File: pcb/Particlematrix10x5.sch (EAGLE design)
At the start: 67 parts, among them IC1 4017D

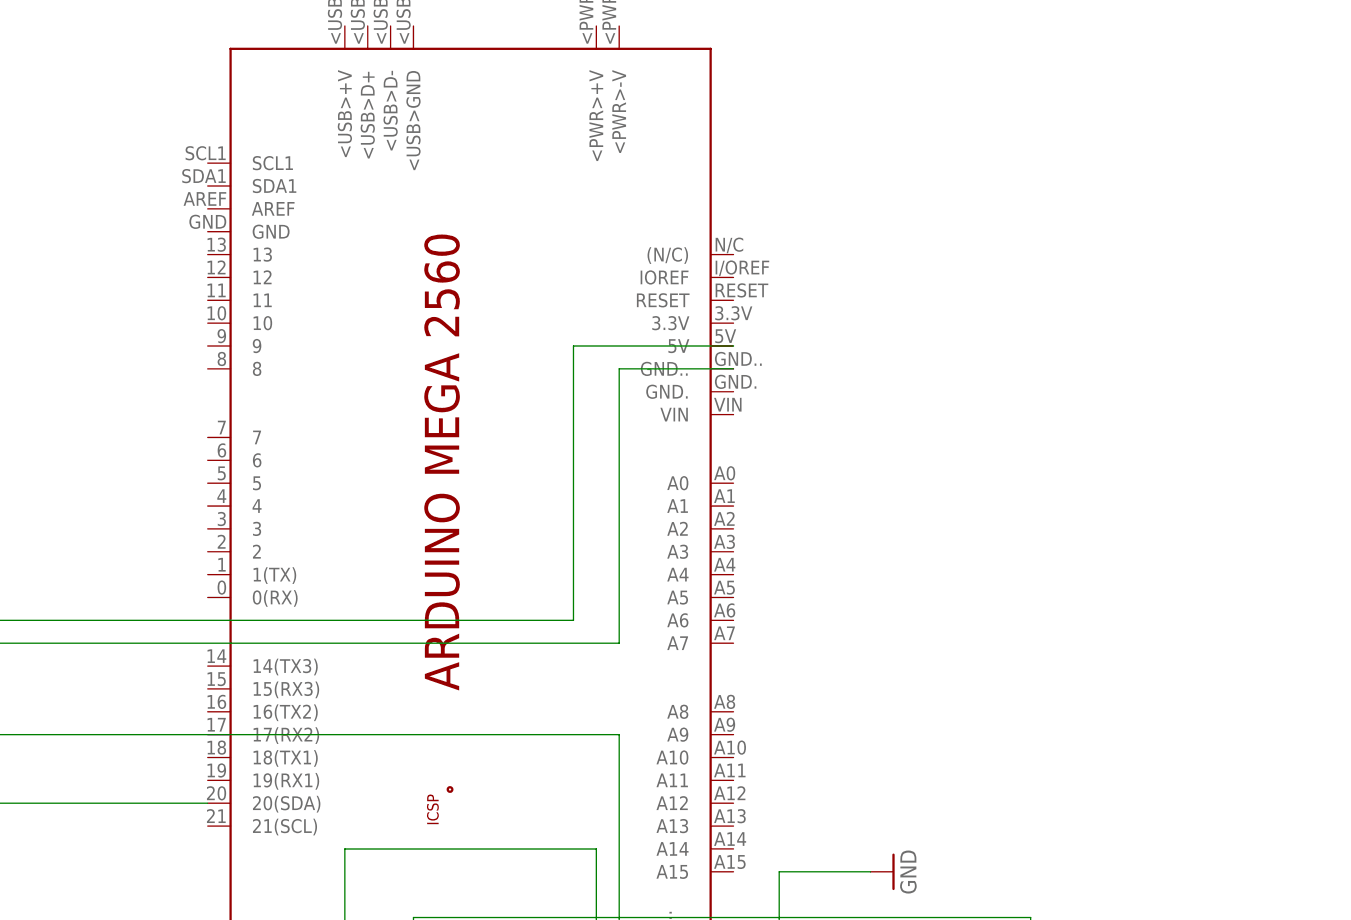
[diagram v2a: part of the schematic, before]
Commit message: Fix routing errors on pcb
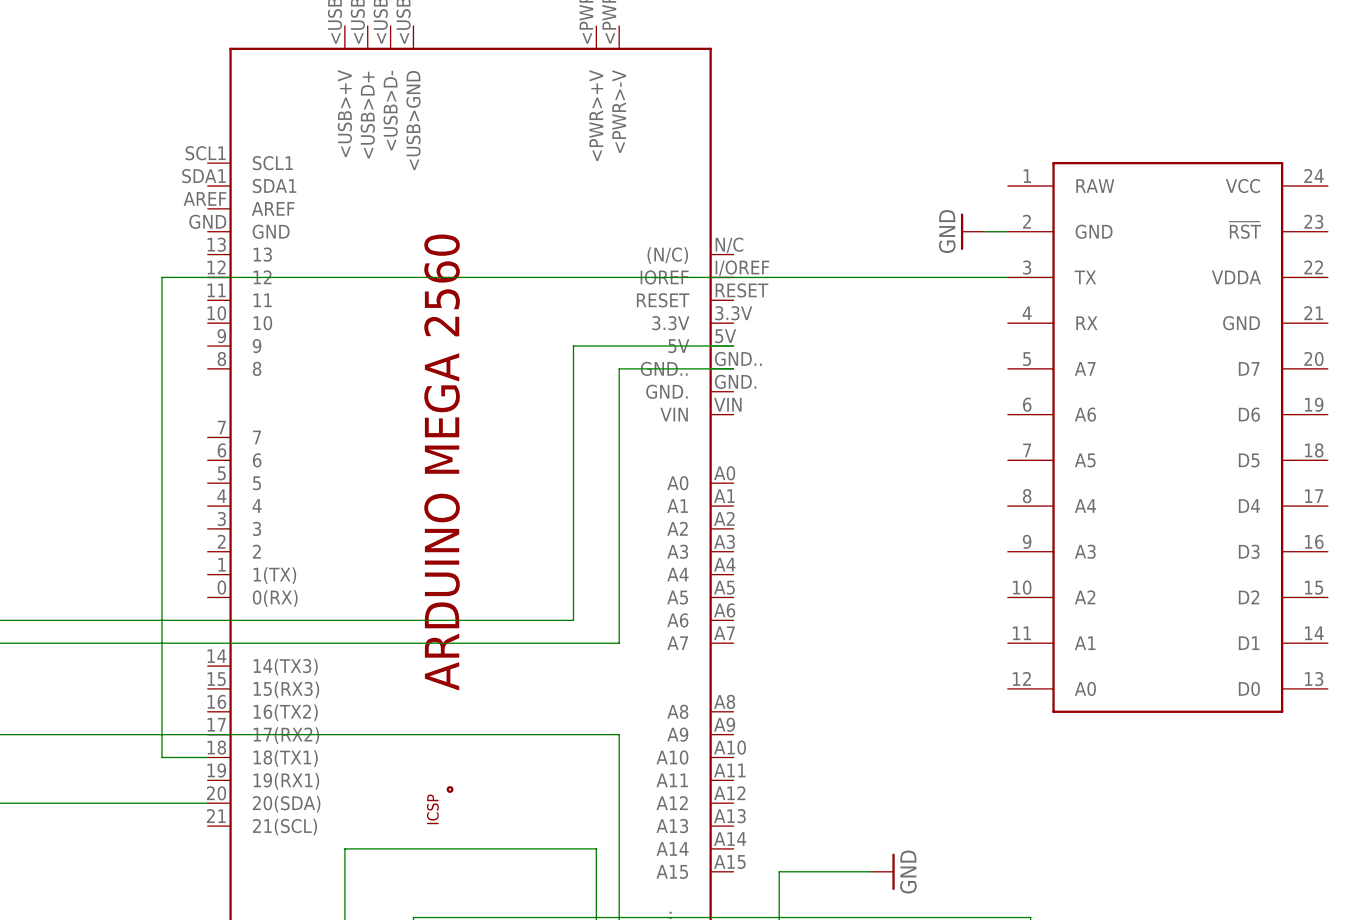
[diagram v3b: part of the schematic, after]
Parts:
- added U$1: SPARK_CORECORE, Spark:SPARK_CORECORE
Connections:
- new net N$10: PCB1.18(TX1), U$1.TX
- net GND: now also U$1.GND@2
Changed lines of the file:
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@@
 <part name="GND5" library="supply1" deviceset="GND" device=""/>
 <part name="GND6" library="supply1" deviceset="GND" device=""/>
+<part name="U$1" library="Spark" deviceset="SPARK_CORE" device="CORE"/>
+<part name="GND7" library="supply1" deviceset="GND" device=""/>
 </parts>
 <sheets>
@@
 <instance part="GND6" gate="1" x="210.82" y="205.74" rot="R90"/>
 <instance part="IC1" gate="P" x="68.58" y="157.48"/>
+<instance part="U$1" gate="G$1" x="241.3" y="254"/>
+<instance part="GND7" gate="1" x="218.44" y="276.86" rot="R270"/>
 </instances>
 <busses>
@@
 <junction x="185.42" y="190.5"/>
 </segment>
+<segment>
+<pinref part="U$1" gate="G$1" pin="GND@2"/>
+<wire x1="223.52" y1="276.86" x2="220.98" y2="276.86" width="0.1524" layer="91"/>
+<pinref part="GND7" gate="1" pin="GND"/>
+</segment>
 </net>
 <net name="N$8" class="0">
@@
 </segment>
 </net>
+<net name="N$10" class="0">
+<segment>
+<pinref part="U$1" gate="G$1" pin="TX"/>
+<wire x1="223.52" y1="271.78" x2="129.54" y2="271.78" width="0.1524" layer="91"/>
+<wire x1="129.54" y1="271.78" x2="129.54" y2="218.44" width="0.1524" layer="91"/>
+<pinref part="PCB1" gate="G$1" pin="18(TX1)"/>
+<wire x1="129.54" y1="218.44" x2="134.62" y2="218.44" width="0.1524" layer="91"/>
+</segment>
+</net>

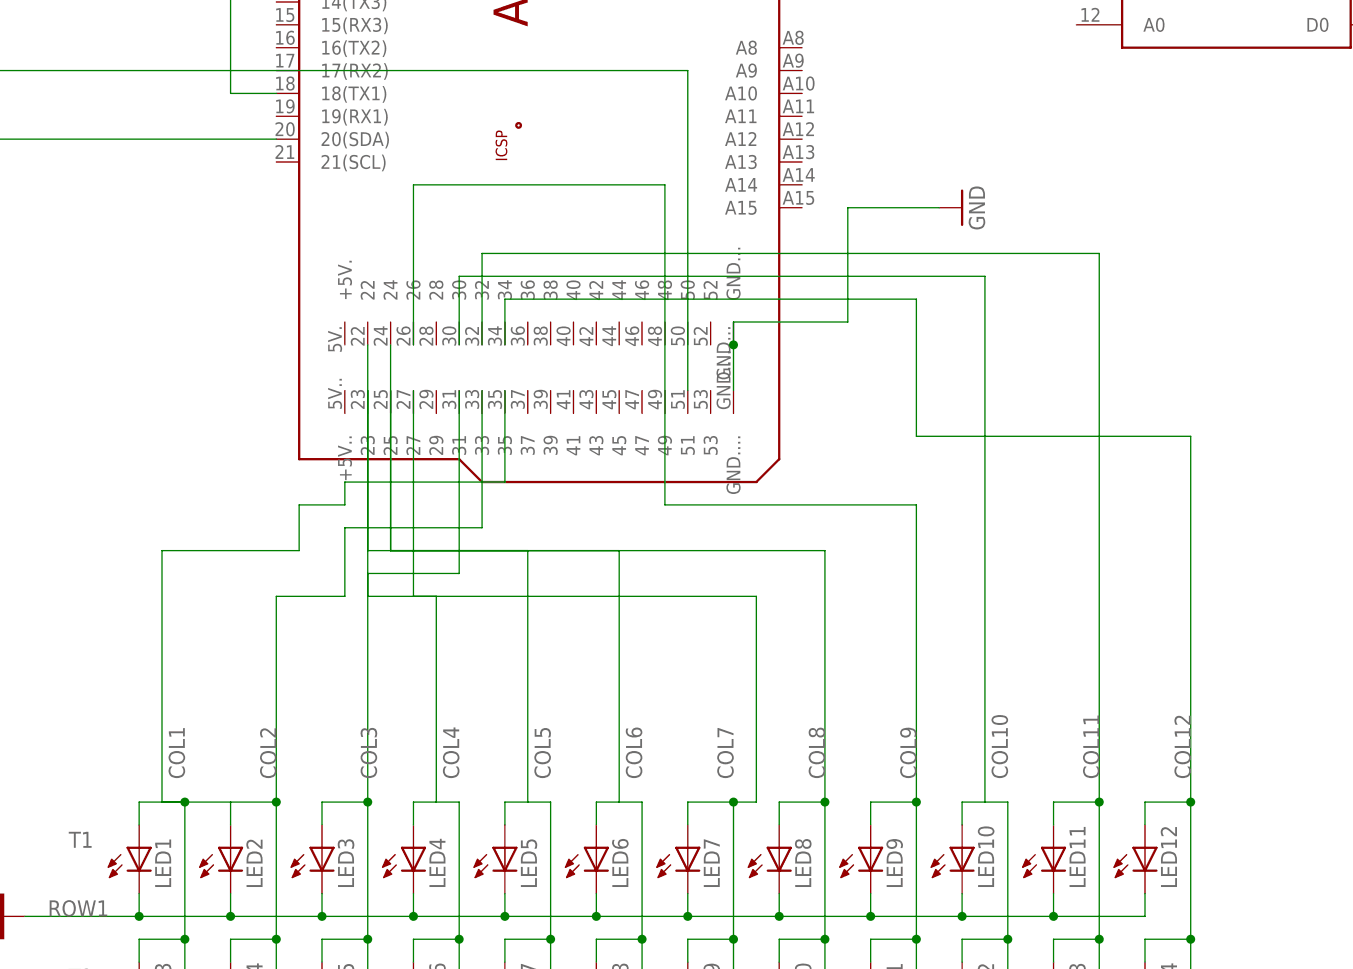
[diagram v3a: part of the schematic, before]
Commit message: Mirrored Arduino and Spark Core again to face front; rerouted
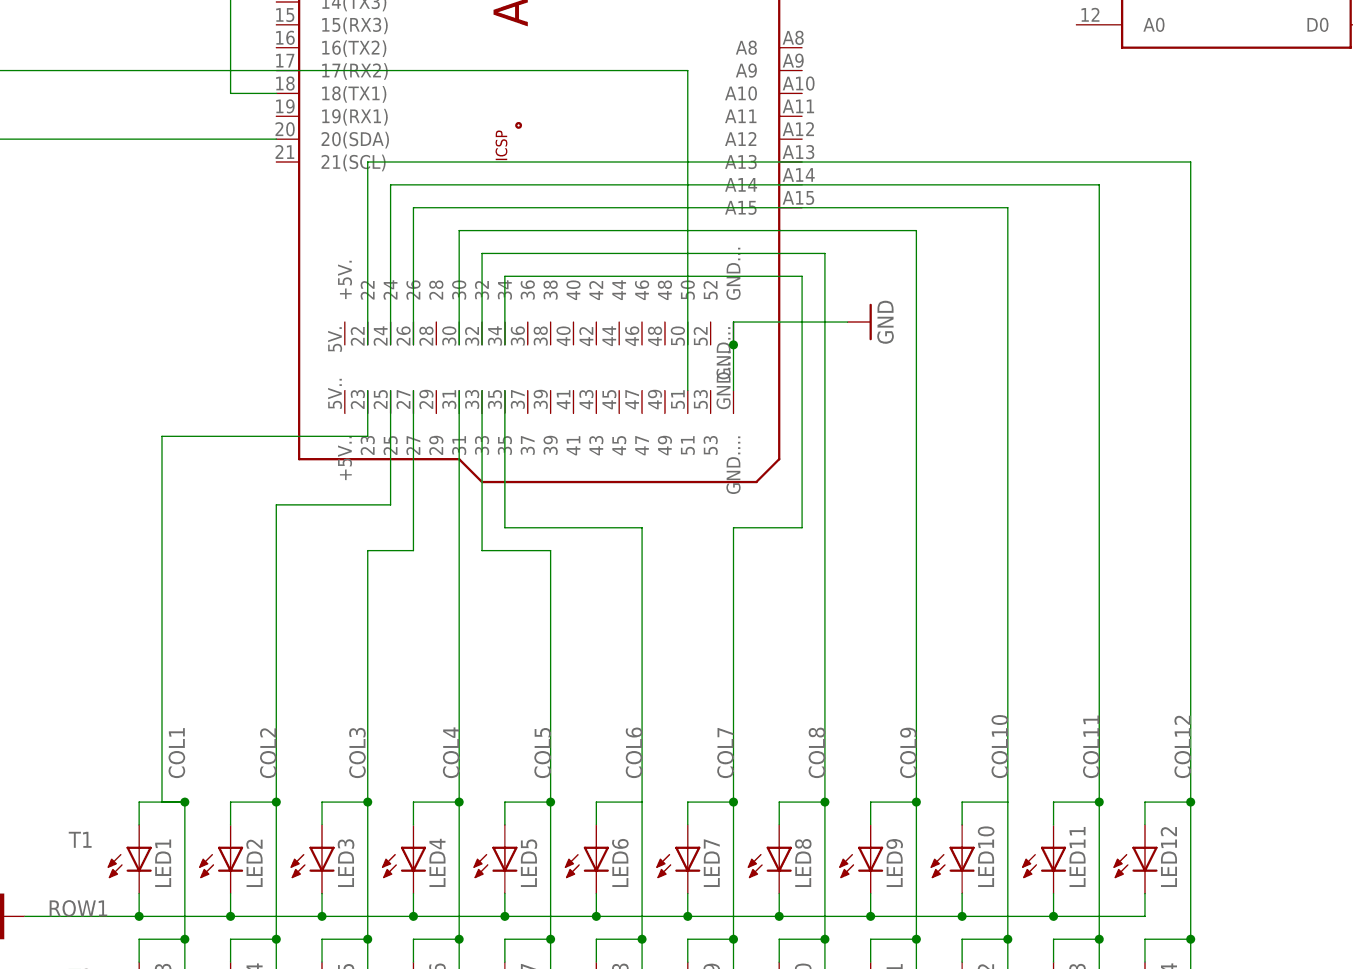
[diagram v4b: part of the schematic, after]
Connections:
- net COL1: now also PCB1.23; no longer PCB1.35
- net COL10: now also PCB1.26; no longer PCB1.30
- net COL11: now also PCB1.24; no longer PCB1.32
- net COL12: now also PCB1.22; no longer PCB1.34
- net COL2: now also PCB1.25; no longer PCB1.33
- net COL3: now also PCB1.27; no longer PCB1.31
- net COL4: now also PCB1.31; no longer PCB1.27
- net COL5: now also PCB1.33; no longer PCB1.25
- net COL6: now also PCB1.35; no longer PCB1.23
- net COL7: now also PCB1.34; no longer PCB1.22
- net COL8: now also PCB1.32; no longer PCB1.24
- net COL9: now also PCB1.30; no longer PCB1.26

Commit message: Cleanup in schematic
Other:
- moved on the sheet: IC1P
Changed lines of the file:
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@@
 <instance part="GND5" gate="1" x="101.6" y="58.42"/>
 <instance part="GND6" gate="1" x="200.66" y="193.04" rot="R90"/>
-<instance part="IC1" gate="P" x="68.58" y="157.48"/>
-<instance part="U$1" gate="G$1" x="241.3" y="254"/>
-<instance part="GND7" gate="1" x="218.44" y="276.86" rot="R270"/>
+<instance part="IC1" gate="P" x="205.74" y="261.62"/>
+<instance part="U$1" gate="G$1" x="104.14" y="289.56" rot="R180"/>
+<instance part="GND7" gate="1" x="124.46" y="266.7" rot="R90"/>
 </instances>
 <busses>
@@
 <segment>
 <pinref part="U$1" gate="G$1" pin="GND@2"/>
-<wire x1="223.52" y1="276.86" x2="220.98" y2="276.86" width="0.1524" layer="91"/>
 <pinref part="GND7" gate="1" pin="GND"/>
 </segment>
@@
 <net name="N$6" class="0">
 <segment>
+<pinref part="PCB1" gate="G$1" pin="5V"/>
+<wire x1="193.04" y1="264.16" x2="200.66" y2="264.16" width="0.1524" layer="91"/>
+<wire x1="200.66" y1="264.16" x2="200.66" y2="271.78" width="0.1524" layer="91"/>
 <pinref part="IC1" gate="P" pin="VDD"/>
-<wire x1="68.58" y1="165.1" x2="68.58" y2="231.14" width="0.1524" layer="91"/>
-<wire x1="68.58" y1="231.14" x2="71.12" y2="233.68" width="0.1524" layer="91"/>
-<wire x1="71.12" y1="233.68" x2="175.26" y2="233.68" width="0.1524" layer="91"/>
-<wire x1="175.26" y1="233.68" x2="175.26" y2="264.16" width="0.1524" layer="91"/>
-<pinref part="PCB1" gate="G$1" pin="5V"/>
-<wire x1="175.26" y1="264.16" x2="193.04" y2="264.16" width="0.1524" layer="91"/>
+<wire x1="200.66" y1="271.78" x2="205.74" y2="271.78" width="0.1524" layer="91"/>
+<wire x1="205.74" y1="271.78" x2="205.74" y2="269.24" width="0.1524" layer="91"/>
 </segment>
 </net>
 <net name="N$9" class="0">
 <segment>
+<pinref part="PCB1" gate="G$1" pin="GND.."/>
+<wire x1="193.04" y1="261.62" x2="200.66" y2="261.62" width="0.1524" layer="91"/>
+<wire x1="200.66" y1="261.62" x2="200.66" y2="248.92" width="0.1524" layer="91"/>
 <pinref part="IC1" gate="P" pin="VSS"/>
-<wire x1="68.58" y1="149.86" x2="91.44" y2="149.86" width="0.1524" layer="91"/>
-<wire x1="91.44" y1="149.86" x2="91.44" y2="231.14" width="0.1524" layer="91"/>
-<wire x1="91.44" y1="231.14" x2="180.34" y2="231.14" width="0.1524" layer="91"/>
-<wire x1="180.34" y1="231.14" x2="180.34" y2="261.62" width="0.1524" layer="91"/>
-<pinref part="PCB1" gate="G$1" pin="GND.."/>
-<wire x1="180.34" y1="261.62" x2="193.04" y2="261.62" width="0.1524" layer="91"/>
+<wire x1="200.66" y1="248.92" x2="205.74" y2="248.92" width="0.1524" layer="91"/>
+<wire x1="205.74" y1="248.92" x2="205.74" y2="254" width="0.1524" layer="91"/>
 </segment>
 </net>
@@
 <segment>
 <pinref part="U$1" gate="G$1" pin="TX"/>
-<wire x1="223.52" y1="271.78" x2="129.54" y2="271.78" width="0.1524" layer="91"/>
+<wire x1="121.92" y1="271.78" x2="129.54" y2="271.78" width="0.1524" layer="91"/>
 <wire x1="129.54" y1="271.78" x2="129.54" y2="218.44" width="0.1524" layer="91"/>
 <pinref part="PCB1" gate="G$1" pin="18(TX1)"/>
